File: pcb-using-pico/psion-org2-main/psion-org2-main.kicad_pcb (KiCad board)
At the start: 2 copper layers, 70 x 106 mm, 124 parts, among them J1 Conn_01x24_Female, J2 Conn_01x03_Female, J3 Conn_01x27_Female, J4 Conn_01x02_Female, J5 Conn_01x02_Female, J6 Conn_01x11_Female, M1 P-CHANNEL-MOSFET, M2 P-CHANNEL-MOSFET, M3 P-CHANNEL-MOSFET, SW1 AC_ON, SW10 n, SW11 t, SW12 del, SW13 up, SW14 c, SW15 i, SW16 o, SW17 u, SW18 y, SW19 down, SW2 A, SW20 d, SW21 j, SW22 p, SW23 v, SW24 z, SW25 left, SW26 e, SW27 k, SW28 q, SW29 w, SW3 g, SW30 spc, SW31 right, SW32 f, SW33 L, SW34 r, SW35 x, SW36 exe, SW4 m, SW5 s, SW6 shft, SW7 mode, SW8 b, SW9 h, U1 Pico, U10 AMS1117-3.3, U2 74HC595, U3 Regulator_Switching_MT3608, U4 74LS165, U5 74HC595, U6 AMS1117-5.0, U7 MCP7940N-xSN, Y1 32k768Hz

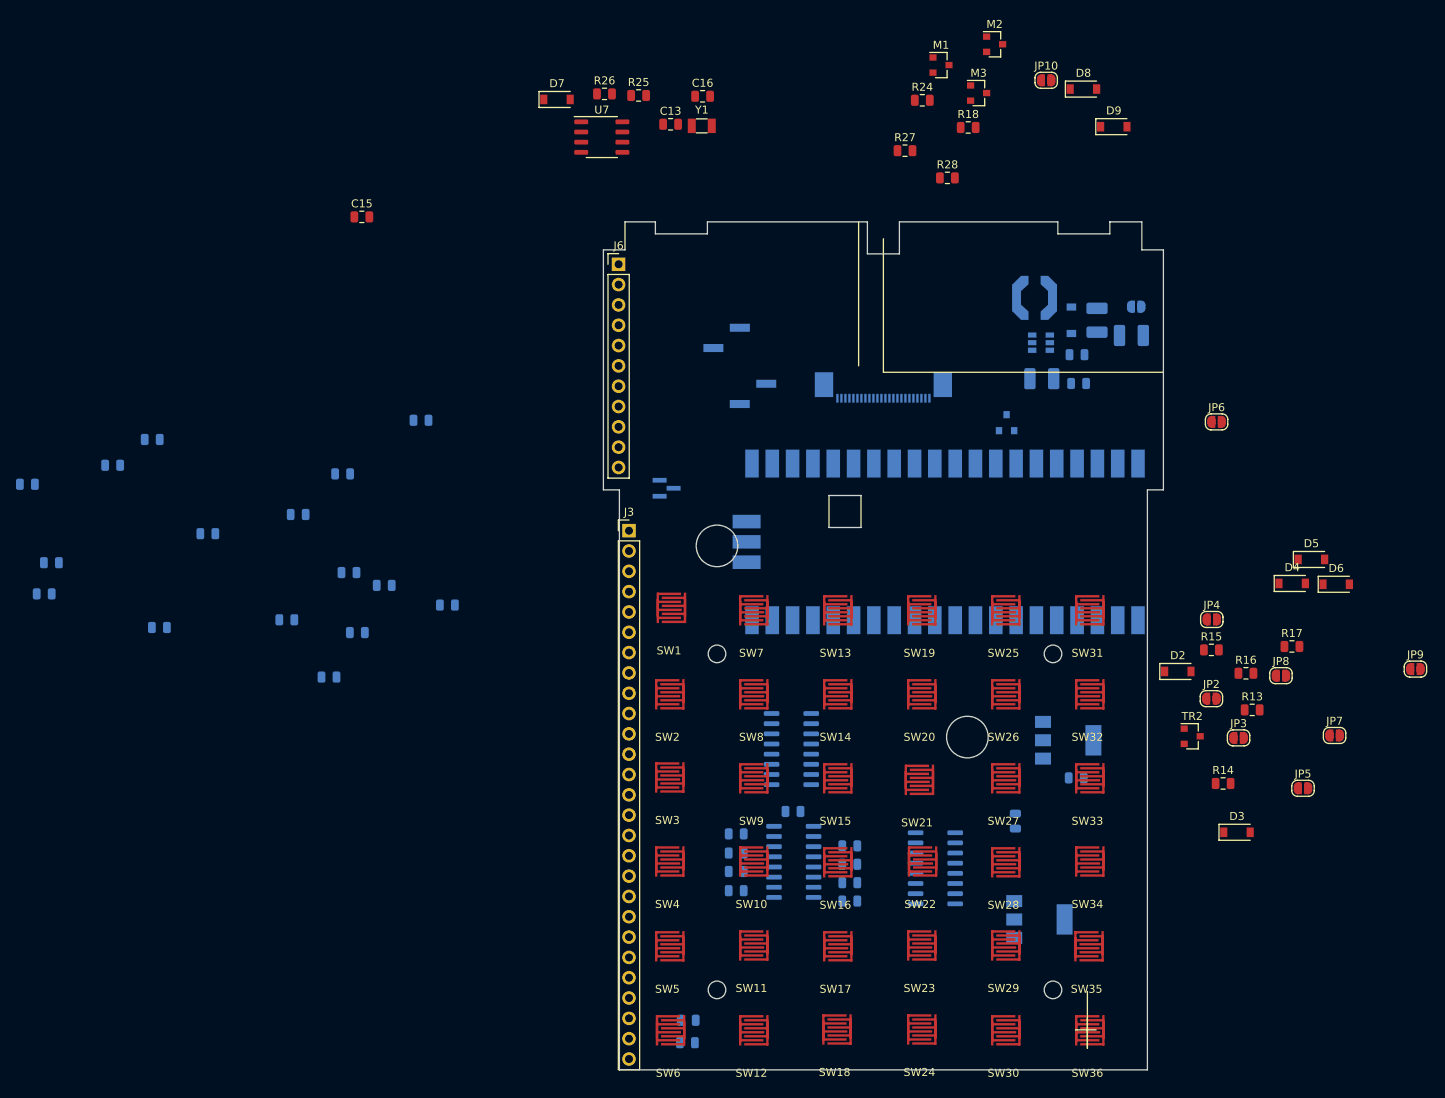
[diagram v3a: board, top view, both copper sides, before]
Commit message: First main PCB layout
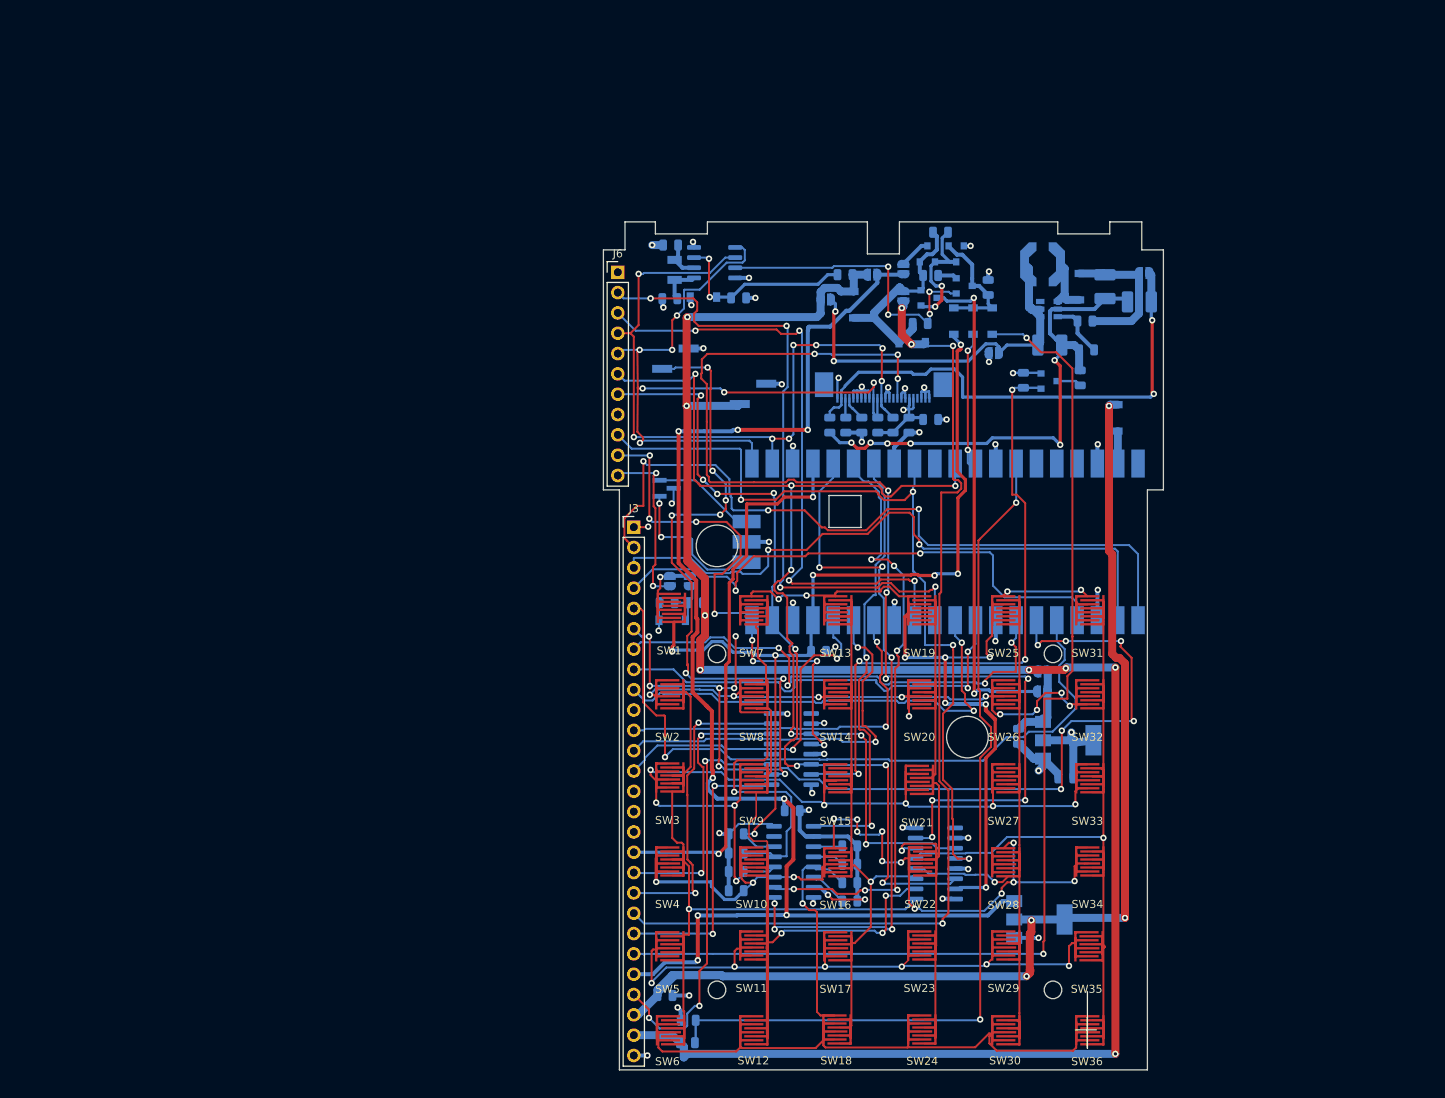
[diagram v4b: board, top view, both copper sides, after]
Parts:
- removed C11, C12, C6, C7, C8, C9: 100n, Capacitor_SMD:C_0805_2012Metric
- removed C5: 1u, Capacitor_SMD:C_0805_2012Metric
- removed R25, R26: 4k7, Resistor_SMD:R_0805_2012Metric
- C13, C15, C16, D2, D3, D4, D5, D6, D7, D8, D9, JP10, JP2, JP3, JP4, JP5, JP6, JP7, JP8, JP9, M1, M2, M3, R13, R14, R15, R16, R17, R18, R24, R27, R28, TR2, U7, Y1: moved to B.Cu
- moved R3 108.5 mm to (174.5, 81.1), turned to 90 degrees
- moved R4 104.7 mm to (172.6, 81.1), turned to 90 degrees
- moved C15 104.4 mm to (146.0, 152.4)
- moved R10 99.2 mm to (197.9, 75.2), turned to 90 degrees
- moved JP9 91.4 mm to (149.1, 100.6), turned to 90 degrees
- moved R1 91.3 mm to (165.2, 109.4)
- moved D6 83.1 mm to (146.9, 105.5), turned to 180 degrees
- moved JP7 81.6 mm to (171.9, 62.3)
- moved R17 78.3 mm to (146.3, 103.3), turned to 180 degrees
- moved R14 77.4 mm to (180.4, 57.0)
- moved JP8 77.3 mm to (146.6, 100.6), turned to 90 degrees
- moved JP3 75.3 mm to (166.1, 65.4)
- moved C1 73.7 mm to (176.5, 81.1), turned to 270 degrees
- moved D3 73.1 mm to (182.1, 68.1), turned to 270 degrees
- moved C3 71.4 mm to (179.2, 80.4)
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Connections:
- J3 pad 11: (no net) -> SCLK
- J3 pad 12: (no net) -> SOE
- J3 pad 13: (no net) -> SMR
- J3 pad 2: (no net) -> SD0
- J3 pad 3: (no net) -> SD1
- J3 pad 4: (no net) -> SD2
- J3 pad 5: (no net) -> SD3
- J3 pad 6: (no net) -> SD4
- J3 pad 7: (no net) -> SD5
- J3 pad 8: (no net) -> SD6
- J3 pad 9: (no net) -> SD7
- U1 pad 1: (no net) -> SD0
- U1 pad 10: (no net) -> SD7
- U1 pad 14: (no net) -> SCLK
- U1 pad 15: (no net) -> SOE
- U1 pad 16: (no net) -> SMR
- U1 pad 2: (no net) -> SD1
- U1 pad 4: (no net) -> SD2
- U1 pad 5: (no net) -> SD3
- U1 pad 6: (no net) -> SD4
- U1 pad 7: (no net) -> SD5
- U1 pad 9: (no net) -> SD6
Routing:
- net VBAT: track 0.00 -> 245.6 mm, vias 0 -> 8
- net 5V: track 0.00 -> 193.7 mm, vias 0 -> 4
- net VBAT_SWITCHED2: track 0.00 -> 173.4 mm, vias 0 -> 8
- net P55: track 0.00 -> 146.5 mm, vias 0 -> 8
- net GND: track 0.00 -> 145.3 mm, vias 0 -> 42
- net P56: track 0.00 -> 145.3 mm, vias 0 -> 11
- net OLED_RES: track 0.00 -> 144.5 mm, vias 0 -> 10
- net EX_ON: track 0.00 -> 139.4 mm, vias 0 -> 2
- net P52: track 0.00 -> 134.4 mm, vias 0 -> 1
- net K1: track 0.00 -> 133.9 mm, vias 0 -> 10
- net SCLKOUT: track 0.00 -> 128.4 mm, vias 0 -> 7
- net EXT_PWR_IN: track 0.00 -> 126.5 mm, vias 0 -> 4
- net K3: track 0.00 -> 123.8 mm, vias 0 -> 3
- net SD4: track 0.00 -> 123.2 mm, vias 0 -> 12
- net P54: track 0.00 -> 121.9 mm, vias 0 -> 14
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- added copper zone on In2.Cu, net +3V3
- added copper zone on In1.Cu, net GND
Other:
- copper layers 2 -> 4
- board text added: "BUZ"
- board text added: "GND"
- board text added: "SWCLK"
- board text added: "SWD"
- board text added: "VBAT"

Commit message: First layouts for fabrication
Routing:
- net GND: track 145.3 -> 561.5 mm, vias 42 -> 71
- net +3V3: track 57.4 -> 347.4 mm, vias 12 -> 33
- net PICO_RX: track 76.4 -> 81.9 mm
- net SCLKIN: track 74.5 -> 77.1 mm
- net P52: track 134.4 -> 132.2 mm, vias 1 -> 3
- net LATCHOUT2: track 67.7 -> 69.9 mm
- net P56: track 145.3 -> 147.1 mm, vias 11 -> 13
- net VBAT_SWITCHED2: track 173.4 -> 174.4 mm
- added copper zone on B.Cu, net +3V3
- added copper zone on F.Cu, net GND
- removed copper zone on In2.Cu, net +3V3
- removed copper zone on In1.Cu, net GND
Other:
- copper layers 4 -> 2

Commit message: Small updates and sent to fab
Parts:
- moved D9 7.04 mm to (169.9, 69.7)
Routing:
- net EXT_PWR_IN: track 126.9 -> 207.3 mm
- net K7: track 107.3 -> 104.7 mm
- net K1: track 133.9 -> 133.0 mm
- net Net-(D8-Pad1): track 27.1 -> 27.7 mm
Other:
- board text added: "Psion Organiser 2 Re Creation Main Board menadue@gmail.com Nov 2021 V1.0"

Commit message: V1.1 started
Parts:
- removed C14, C15: 100n, Capacitor_SMD:C_0805_2012Metric
- removed JP10, JP8, JP9: Jumper_NO_Small, Jumper:SolderJumper-2_P1.3mm_Open_RoundedPad1.0x1.5mm
- removed U6: AMS1117-5.0, Package_TO_SOT_SMD:SOT-223-3_TabPin2
- added C5: C_Small, Capacitor_SMD:C_0805_2012Metric, F.Cu at (232.9, 79.5)
- added C6: C_Small, Capacitor_SMD:C_0805_2012Metric, F.Cu at (217.2, 97.7)
- added C7: C_Small, Capacitor_SMD:C_0805_2012Metric, F.Cu at (233.3, 100.5)
- added D10: 4v7, Diode_SMD:D_SOD-123, F.Cu at (222.8, 96.1)
- added D11: 4v7, Diode_SMD:D_SOD-123, F.Cu at (217.5, 81.1)
- added D12: 1N4148, Diode_SMD:D_SOD-123, F.Cu at (215.1, 90.6)
- added D13: 1N4148, Diode_SMD:D_SOD-123, F.Cu at (231.4, 94.7)
- added D14: 1N4148, Diode_SMD:D_SOD-123, F.Cu at (225.1, 80.2)
- added D15: 1N4148, Diode_SMD:D_SOD-123, F.Cu at (217.7, 86.2)
- added D16: 1N4148, Diode_SMD:D_SOD-123, B.Cu at (193.1, 136.2)
- added D17: 1N4148, Diode_SMD:D_SOD-123, F.Cu at (231.1, 84.5)
- added D18: 1N4148, Diode_SMD:D_SOD-123, F.Cu at (230.9, 75.6)
- added R25: 10k, Resistor_SMD:R_0805_2012Metric, F.Cu at (225.5, 90.6)
- D6: value 4v7 -> 2v7
- D7: value 4v7 -> nopop
- M1: value P-CHANNEL-MOSFET -> P-CH-MOSFET
- R10: value 49R -> 110k; moved to F.Cu
- R11: value 120k -> 110k
- R12: value 18k -> 4k7
- R13, R14: value R_Small -> 100k
- R15: value R_Small -> 100k; moved to F.Cu
- R16: value R_Small -> 2k2
- R17: value R_Small -> nopop
- R18, R24, R27: value R_Small -> 110k
- R28: value R_Small -> 47k
- R3, R4: value 10k -> 2k
- TR1: value Si2302CDS-n-channel -> Si2302CDS-n-ch; moved to F.Cu
- moved TR1 28.8 mm to (222.8, 75.8)
- moved R10 26.9 mm to (223.1, 84.5), turned to 0 degrees
- moved R15 22.4 mm to (213.2, 76.0), turned to 0 degrees
- moved J6 1.25 mm to (140.7, 63.1)
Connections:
- C10 pad 2: Net-(C10-Pad2) -> GND
- C21 pad 2: Net-(C10-Pad2) -> GND
- C22 pad 2: Net-(C10-Pad2) -> GND
- C4 pad 2: Net-(C10-Pad2) -> GND
- D6 pad 1: Net-(D6-Pad1) -> P57
- D8 pad 1: Net-(D8-Pad1) -> VBAT
- D8 pad 2: VBAT -> BATCON
- D9 pad 1: Net-(D8-Pad1) -> VBAT
- J1 pad 10: (no net) -> GND
- J3 pad 10: (no net) -> SPGM
- J3 pad 14: (no net) -> BUZZER
- J3 pad 15: (no net) -> VBAT_SWITCHED1
- J5 pad 1: VBAT -> BATCON
- J6 pad 8: (no net) -> QH_O
- M1 pad 1: RTC_MFP -> Net-(D10-Pad2)
- M2 pad 1: Net-(M2-Pad1) -> Net-(D11-Pad2)
- M2 pad 2: Net-(D8-Pad1) -> VBAT
- M3 pad 1: Net-(M2-Pad1) -> Net-(D11-Pad2)
- M3 pad 2: Net-(D8-Pad1) -> VBAT
- R10 pad 2: Net-(C10-Pad2) -> Net-(D10-Pad2)
- R12 pad 2: Net-(C10-Pad2) -> GND
- R14 pad 1: Net-(D8-Pad1) -> VBAT
- R14 pad 2: Net-(M2-Pad1) -> Net-(D11-Pad2)
- R15 pad 1: DRV_HV -> Net-(D11-Pad2)
- R15 pad 2: GND -> Net-(R15-Pad2)
- R16 pad 1: VBAT -> Net-(R16-Pad1)
- R16 pad 2: Net-(D6-Pad1) -> P57
- R17 pad 1: Net-(D6-Pad1) -> P57
- R18 pad 1: Net-(D8-Pad1) -> VBAT
- R18 pad 2: RTC_MFP -> Net-(D10-Pad2)
- R24 pad 1: Net-(D8-Pad1) -> VBAT
- SW1 pad 1: Net-(JP8-Pad2) -> VBAT
- SW1 pad 2: P57 -> Net-(R16-Pad1)
- SW11 pad 1: p53 -> P53
- SW13 pad 2: K4 -> P53
- SW17 pad 1: p53 -> P53
- SW19 pad 2: K7 -> P54
- SW23 pad 1: p53 -> P53
- SW25 pad 2: K5 -> P55
- SW29 pad 1: p53 -> P53
- SW31 pad 2: K6 -> P56
- SW35 pad 1: p53 -> P53
- SW5 pad 1: p53 -> P53
- SW7 pad 2: K3 -> P52
- TR1 pad 1: DRV_HV -> RTC_MFP
- TR2 pad 3: Net-(M2-Pad1) -> Net-(R15-Pad2)
- U2 pad 1: K2 -> Net-(D13-Pad2)
- U2 pad 15: K1 -> Net-(D12-Pad2)
- U2 pad 2: K3 -> Net-(D14-Pad2)
- U2 pad 3: K4 -> Net-(D15-Pad2)
- U2 pad 4: K5 -> Net-(D16-Pad2)
- U2 pad 5: K6 -> Net-(D17-Pad2)
- U2 pad 6: K7 -> Net-(D18-Pad2)
- U3 pad 2: Net-(C10-Pad2) -> GND
- U5 pad 15: DRV_HV -> (no net)
- U5 pad 4: (no net) -> SPGM
- U5 pad 9: (no net) -> QH_O
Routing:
- net p53: track 104.8 -> 0.00 mm, vias 6 -> 0
- net P53: track 4.83 -> 109.6 mm, vias 0 -> 6
- net DRV_HV: track 79.9 -> 0.00 mm, vias 4 -> 0
- net Net-(C10-Pad2): track 64.1 -> 0.00 mm, vias 6 -> 0
- net GND: track 561.5 -> 610.6 mm, vias 71 -> 75
- net (no net): track 0.00 -> 41.5 mm, vias 0 -> 3
- net VBAT: track 245.6 -> 285.7 mm, vias 8 -> 12
- net BATCON: track 0.00 -> 29.6 mm, vias 0 -> 2
- net Net-(D8-Pad1): track 27.7 -> 0.00 mm
- net Net-(JP8-Pad2): track 14.9 -> 0.00 mm, vias 1 -> 0
- net P57: track 121.4 -> 127.7 mm
- net Net-(D6-Pad1): track 6.26 -> 0.00 mm
- net +3V3: track 347.4 -> 351.9 mm, vias 33 -> 34
- net Net-(R10-Pad1): track 3.12 -> 0.00 mm
- net K5: track 110.6 -> 108.7 mm
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- removed copper zone on B.Cu, net +3V3
- removed copper zone on F.Cu, net GND
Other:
- board text added: "Moved connector, check original to see how PCB outlines line up"
